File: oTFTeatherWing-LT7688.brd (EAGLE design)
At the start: 33 x 50.8 mm, 21 parts, among them U1 SPI Flash

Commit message: minor fixes
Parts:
- added R2: 1M, microbuilder:0603-NO
- C2, C4, C5: value 1uF -> 0.1uF
- R10, R11, R14, R7: value 10K -> 22R
- moved R6 1.14 mm to (32.7, 51.1), turned to 270 degrees
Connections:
- new net LT7688_XI: R2.2, U$1.80
- new net LT7688_XO: R2.1, U$1.1
- net QSPI_DATA[0]: now also U1.2; no longer U1.5
- net QSPI_DATA[1]: now also U1.5; no longer U1.2
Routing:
- net VDD_CAP2: track 65.4 -> 81.3 mm
- net +3V3: track 158.6 -> 174.0 mm
- net BLUE5: track 62.5 -> 69.4 mm
- net GREEN5: track 51.1 -> 56.8 mm
- net LT7688_XI: track 0.00 -> 5.65 mm
- net RED0: track 48.7 -> 54.2 mm
- net LT7688_XO: track 0.00 -> 5.47 mm
- net GREEN0: track 57.8 -> 62.4 mm
- net RED2: track 45.7 -> 50.2 mm
- net GREEN4: track 56.8 -> 61.2 mm
- net RED1: track 49.0 -> 53.3 mm
- net GREEN2: track 58.2 -> 62.4 mm
- net GREEN3: track 59.6 -> 63.8 mm
- net RED5: track 40.8 -> 44.9 mm
- net RED4: track 41.5 -> 45.1 mm
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
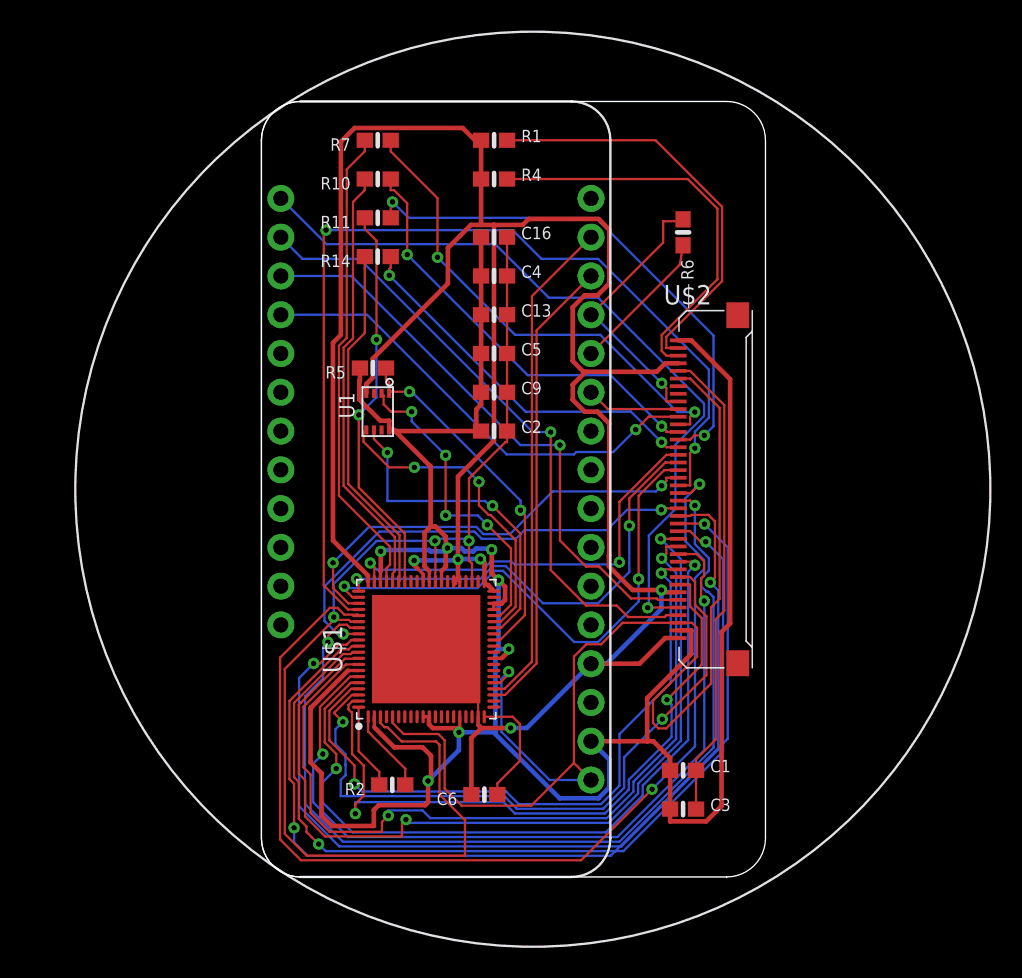
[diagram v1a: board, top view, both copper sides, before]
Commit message: changed lcd spi to lt7688
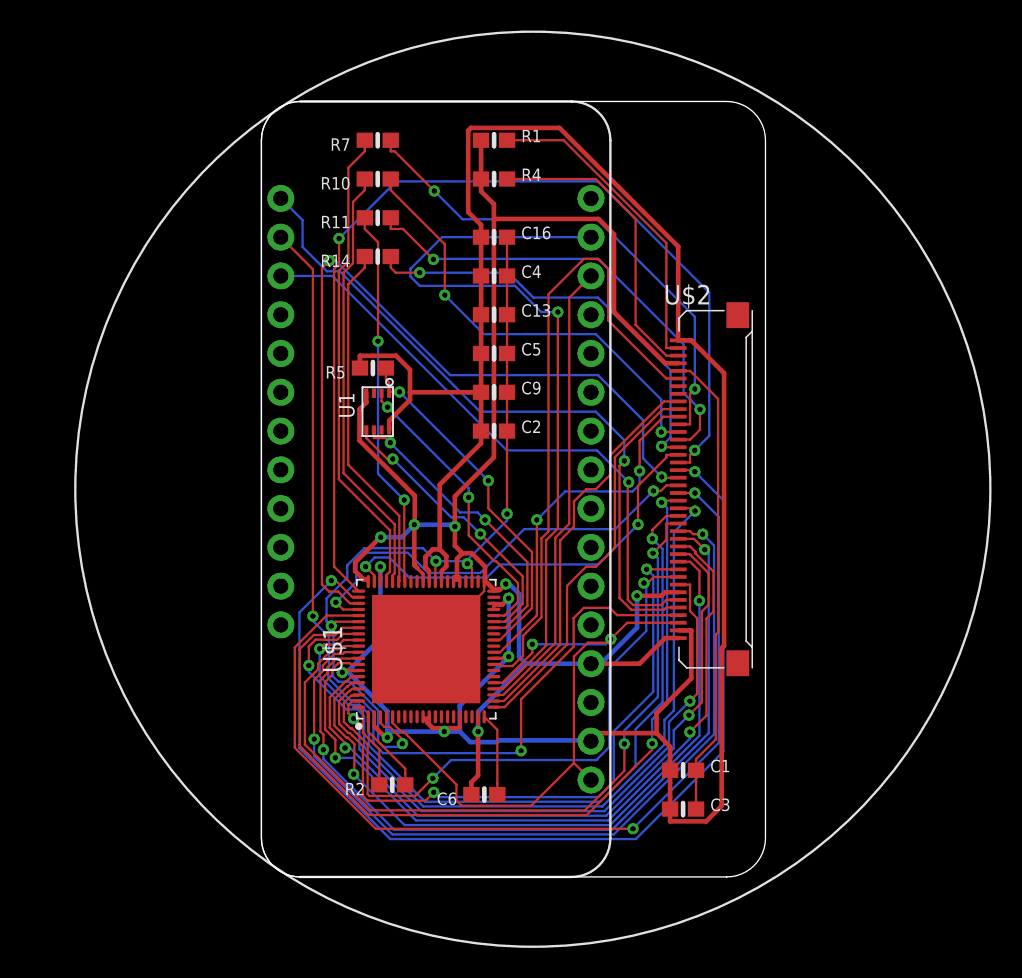
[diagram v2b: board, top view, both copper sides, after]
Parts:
- removed R6: 10K, microbuilder:0603-NO
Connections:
- removed net MISO: MS2.13, R6.1, U$2.9
- removed net MOSI: MS2.12, R6.2
- removed net SCK: MS2.11, U$2.10
- new net LCD_RESET: U$1.28, U$2.6
- new net LCD_SCL: U$1.21, U$2.10
- new net LCD_SDO: U$1.22, U$2.9
- net !RESET: no longer U$2.6
- net LCD_CS: now also U$1.30; no longer MS2.20
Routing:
- net GND: track 169.3 -> 116.3 mm, vias 5 -> 6
- net LCD_RESET: track 0.00 -> 41.3 mm
- net !RESET: track 82.3 -> 41.8 mm, vias 1 -> 2
- net BLUE1: track 29.9 -> 65.1 mm
- net BLUE4: track 64.0 -> 29.1 mm
- net BLUE2: track 34.4 -> 66.9 mm
- net VDD_CAP2: track 81.3 -> 54.1 mm, vias 3 -> 5
- net LCD_SDO: track 0.00 -> 25.9 mm
- net LCD_SCL: track 0.00 -> 25.9 mm
- net BLUE3: track 29.2 -> 54.5 mm
- net SCL: track 41.7 -> 63.6 mm, vias 1 -> 2
- net GREEN1: track 30.5 -> 52.4 mm
- net MISO: track 18.0 -> 0.00 mm, vias 1 -> 0
- net TX: track 32.6 -> 50.6 mm, vias 0 -> 1
- net GREEN2: track 62.4 -> 49.4 mm
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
